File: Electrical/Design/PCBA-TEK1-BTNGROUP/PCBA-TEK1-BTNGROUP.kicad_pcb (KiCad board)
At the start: 4 copper layers, 100 x 45.2 mm, 11 parts, among them J1001 Conn_01x05, J1002 Conn_01x05, SW1001 CPG135001D02, SW1002 CPG135001D02, SW1003 CPG135001D02, SW1004 CPG135001D02, SW1005 CPG135001D02, SW1006 CPG135001D02, SW1007 CPG135001D02, SW1008 CPG135001D02

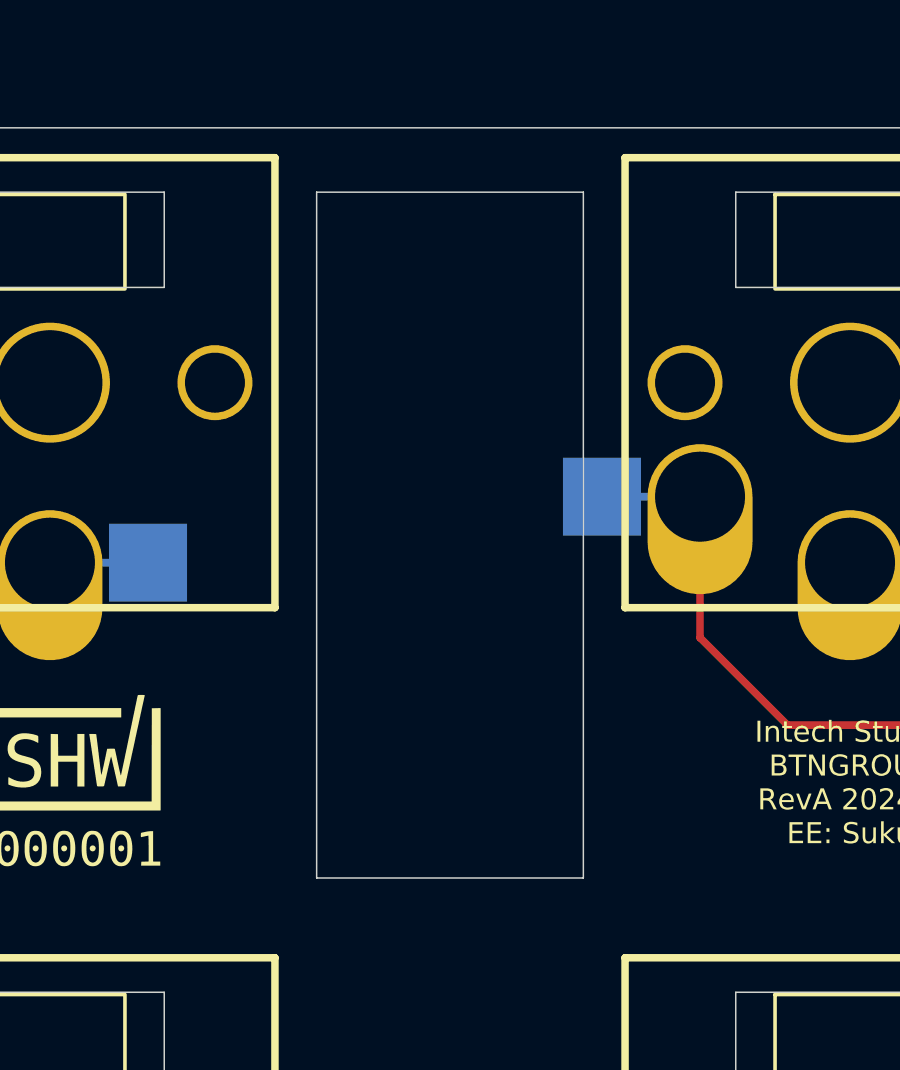
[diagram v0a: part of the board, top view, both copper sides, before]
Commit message: SUKU erc severity for edge clearence fixed
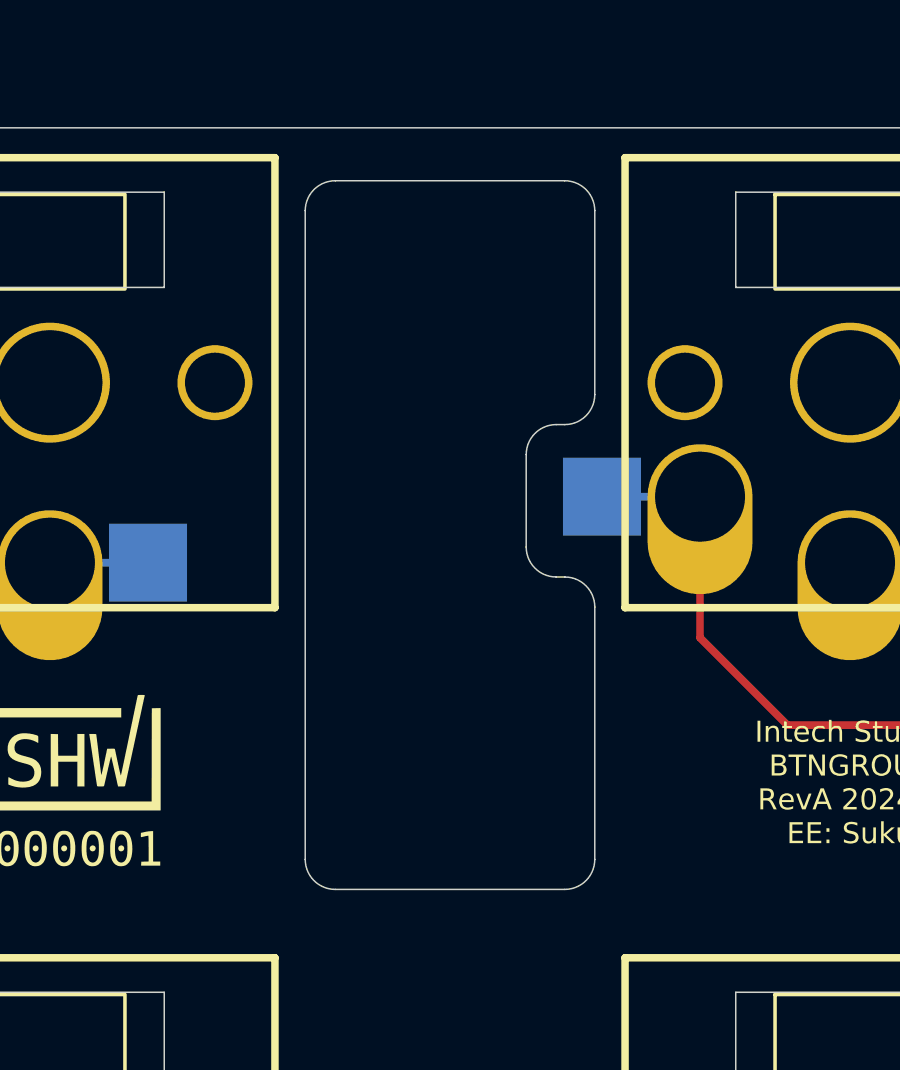
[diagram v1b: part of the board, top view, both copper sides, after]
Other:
- outline, holes or cut-outs redrawn
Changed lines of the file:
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@@
+	)
+	(gr_line
+		(start 96.174 130.226)
+		(end 103.826 130.226)
+		(stroke
+			(width 0.05)
+			(type default)
+		)
+		(layer "Edge.Cuts")
 	)
 	(gr_line
@@
 			(width 0.1)
 			(type solid)
+		)
+		(layer "Edge.Cuts")
+	)
+	(gr_line
+		(start 95.174 107.604)
+		(end 95.174 129.226)
+		(stroke
+			(width 0.05)
+			(type default)
 		)
 		(layer "Edge.Cuts")
@@
 		(layer "Edge.Cuts")
 	)
-	(gr_rect
-		(start 95.555 106.985)
-		(end 104.445 129.845)
-		(stroke
-			(width 0.05)
-			(type default)
-		)
-		(fill none)
-		(layer "Edge.Cuts")
-	)
 	(gr_line
 		(start 104 147.5)
@@
 			(width 0.05)
 			(type solid)
+		)
+		(layer "Edge.Cuts")
+	)
+	(gr_line
+		(start 102.54 118.812)
+		(end 102.54 115.732)
+		(stroke
+			(width 0.05)
+			(type default)
 		)
 		(layer "Edge.Cuts")
@@
 	)
 	(gr_line
+		(start 103.826 106.604)
+		(end 96.174 106.604)
+		(stroke
+			(width 0.05)
+			(type default)
+		)
+		(layer "Edge.Cuts")
+	)
+	(gr_line
 		(start 95 148.5)
 		(end 96 147.5)
@@
 			(width 0.05)
 			(type solid)
+		)
+		(layer "Edge.Cuts")
+	)
+	(gr_line
+		(start 104.826 113.732)
+		(end 104.826 107.604)
+		(stroke
+			(width 0.05)
+			(type default)
 		)
 		(layer "Edge.Cuts")
@@
 		(layer "Edge.Cuts")
 	)
+	(gr_arc
+		(start 96.174 130.226)
+		(mid 95.466893 129.933107)
+		(end 95.174 129.226)
+		(stroke
+			(width 0.05)
+			(type default)
+		)
+		(layer "Edge.Cuts")
+	)
+	(gr_arc
+		(start 102.54 115.732)
+		(mid 102.832893 115.024893)
+		(end 103.54 114.732)
+		(stroke
+			(width 0.05)
+			(type default)
+		)
+		(layer "Edge.Cuts")
+	)
+	(gr_arc
+		(start 103.54 119.812)
+		(mid 102.832893 119.519107)
+		(end 102.54 118.812)
+		(stroke
+			(width 0.05)
+			(type default)
+		)
+		(layer "Edge.Cuts")
+	)
 	(gr_line
 		(start 150 109.34)
@@
 	)
 	(gr_line
+		(start 103.54 114.732)
+		(end 103.826 114.732)
+		(stroke
+			(width 0.05)
+			(type default)
+		)
+		(layer "Edge.Cuts")
+	)
+	(gr_line
 		(start 51.5 147.5)
 		(end 51.5 145.5)
@@
 			(width 0.05)
 			(type solid)
+		)
+		(layer "Edge.Cuts")
+	)
+	(gr_arc
+		(start 103.826 106.604)
+		(mid 104.533107 106.896893)
+		(end 104.826 107.604)
+		(stroke
+			(width 0.05)
+			(type default)
 		)
 		(layer "Edge.Cuts")
@@
 	)
 	(gr_arc
+		(start 103.826 119.812)
+		(mid 104.533107 120.104893)
+		(end 104.826 120.812)
+		(stroke
+			(width 0.05)
+			(type default)
+		)
+		(layer "Edge.Cuts")
+	)
+	(gr_arc
 		(start 122.17 148.5)
 		(mid 122.316447 148.146447)
@@
 		(layer "Edge.Cuts")
 	)
+	(gr_arc
+		(start 95.174 107.604)
+		(mid 95.466893 106.896893)
+		(end 96.174 106.604)
+		(stroke
+			(width 0.05)
+			(type default)
+		)
+		(layer "Edge.Cuts")
+	)
 	(gr_line
 		(start 122.17 148.5)
@@
 		(layer "Edge.Cuts")
 	)
+	(gr_arc
+		(start 104.826 113.732)
+		(mid 104.533107 114.439107)
+		(end 103.826 114.732)
+		(stroke
+			(width 0.05)
+			(type default)
+		)
+		(layer "Edge.Cuts")
+	)
+	(gr_line
+		(start 103.826 119.812)
+		(end 103.54 119.812)
+		(stroke
+			(width 0.05)
+			(type default)
+		)
+		(layer "Edge.Cuts")
+	)
 	(gr_line
 		(start 54.5 148.5)
@@
 		(layer "Edge.Cuts")
 	)
+	(gr_arc
+		(start 104.826 129.226)
+		(mid 104.533107 129.933107)
+		(end 103.826 130.226)
+		(stroke
+			(width 0.05)
+			(type default)
+		)
+		(layer "Edge.Cuts")
+	)
 	(gr_line
 		(start 144 150)
@@
 		)
 		(layer "Edge.Cuts")
+	)
+	(gr_line
+		(start 104.826 129.226)
+		(end 104.826 120.812)
+		(stroke
+			(width 0.05)
+			(type default)
+		)
+		(layer "Edge.Cuts")

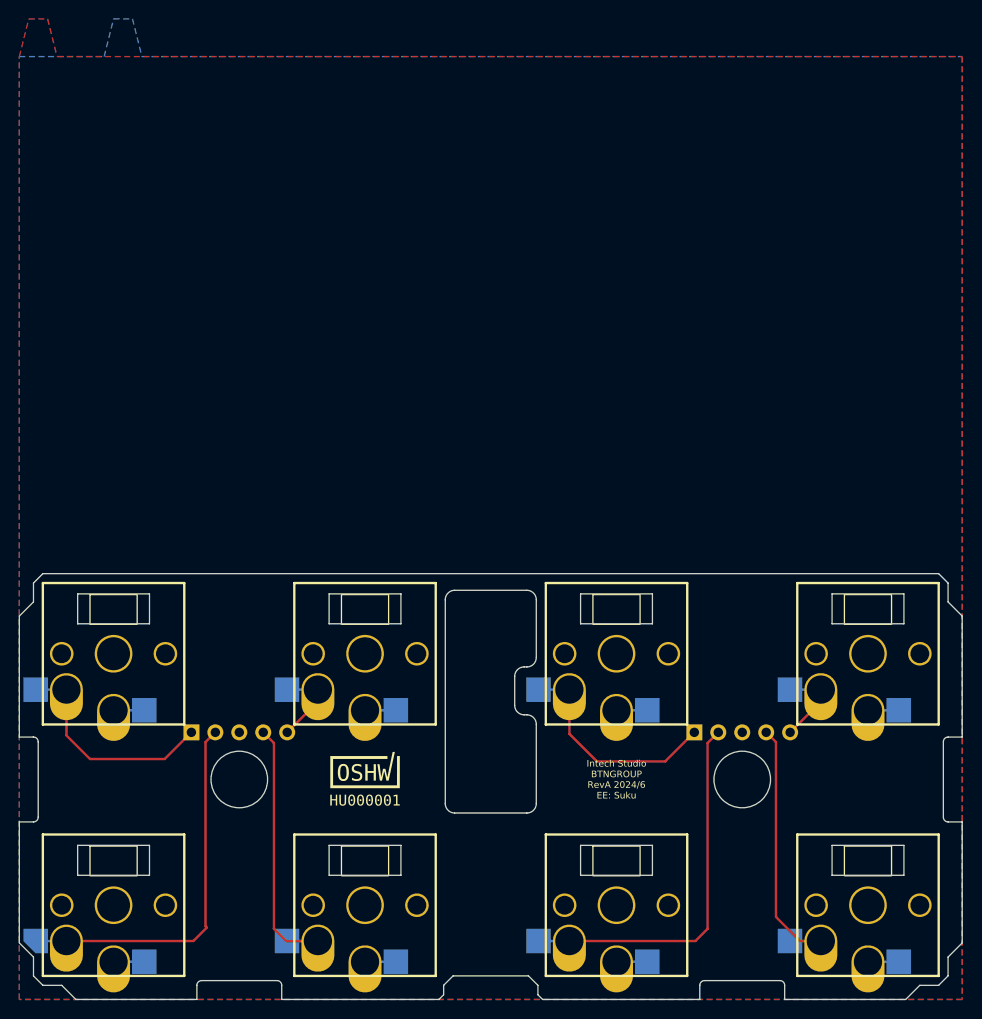
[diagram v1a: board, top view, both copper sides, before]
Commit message: SUKU btn group pcb updated
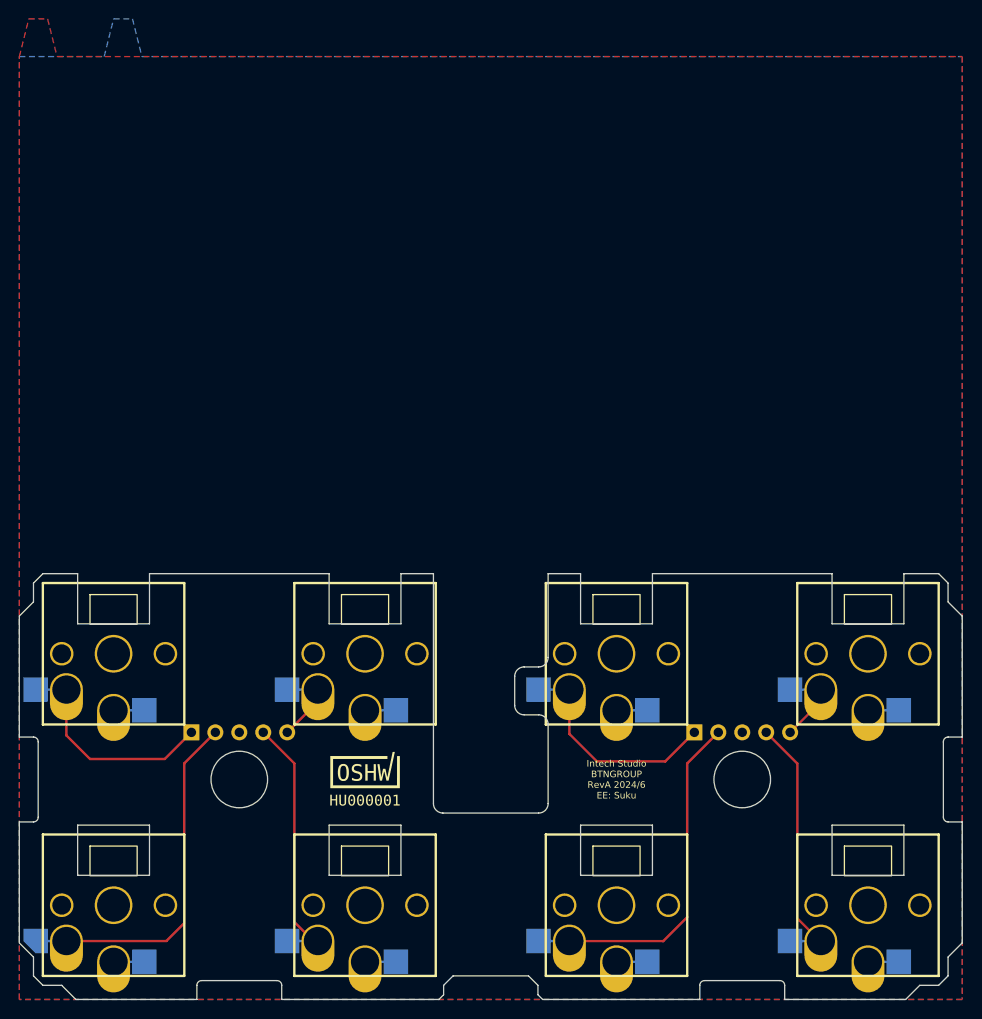
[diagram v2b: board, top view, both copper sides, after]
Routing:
- net Net-(J1002-Pin_2): track 39.8 -> 37.8 mm
- net Net-(J1001-Pin_2): track 39.9 -> 38.2 mm
- net Net-(J1001-Pin_4): track 29.8 -> 28.1 mm
- net Net-(J1002-Pin_4): track 29.1 -> 27.9 mm
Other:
- outline, holes or cut-outs redrawn

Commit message: SUKU buttongroup modified for better clearance
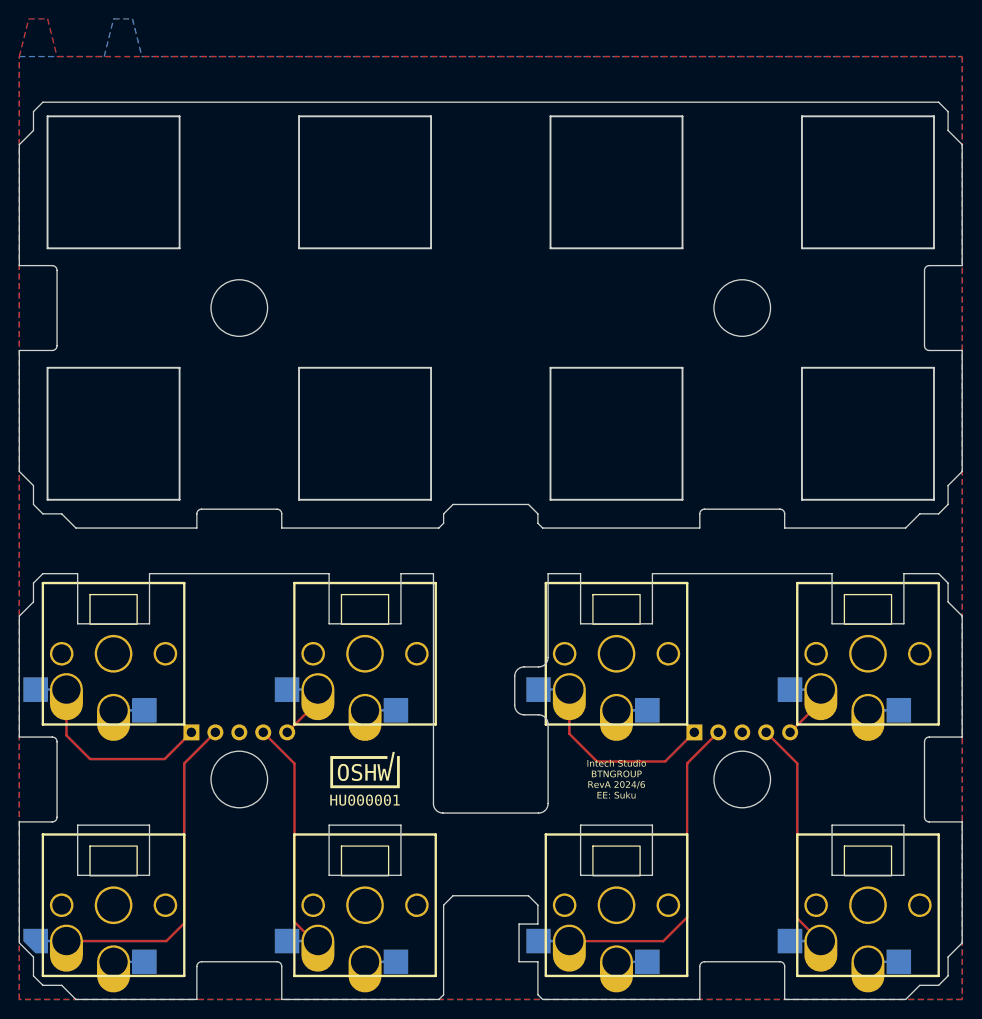
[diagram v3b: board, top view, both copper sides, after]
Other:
- board size 100 x 45.2 mm -> 100 x 95.2 mm

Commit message: SUKU minor outline tweeks
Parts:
- added LOGO701: LOGO, suku_basics:OSHWA, F.Cu at (86.5, 76.7)
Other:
- outline, holes or cut-outs redrawn
- copper layers 4 -> 2
- board text added: "Intech Studio BTNGROUP RevA 2024/7 EE: Suku"
- board text removed: "Intech Studio BTNGROUP RevA 2024/6 EE: Suku"
